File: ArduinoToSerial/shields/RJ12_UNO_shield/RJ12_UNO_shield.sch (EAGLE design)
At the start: 15 parts, among them CON1 RJ12, CON2 RJ12, CON3 RJ12, CON4 RJ12

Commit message: increased isolate space from GND plate. Fixed RX-TX connection
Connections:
- net N$15: now also U$5.TX; no longer U$5.RX
- net N$16: now also U$5.RX; no longer U$5.TX
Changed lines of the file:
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@@
 <segment>
 <pinref part="D0-D7" gate="G$1" pin="D0(RX)"/>
-<pinref part="U$5" gate="G$1" pin="RX"/>
-<wire x1="58.42" y1="0" x2="106.68" y2="0" width="0.1524" layer="91"/>
 <pinref part="D0-D1" gate="G$1" pin="D0(RX)"/>
 <wire x1="106.68" y1="0" x2="124.46" y2="0" width="0.1524" layer="91"/>
-<junction x="106.68" y="0"/>
+<pinref part="U$5" gate="G$1" pin="TX"/>
+<wire x1="58.42" y1="5.08" x2="76.2" y2="5.08" width="0.1524" layer="91"/>
+<wire x1="76.2" y1="5.08" x2="81.28" y2="0" width="0.1524" layer="91"/>
+<wire x1="81.28" y1="0" x2="106.68" y2="0" width="0.1524" layer="91"/>
 </segment>
 </net>
@@
 <segment>
 <pinref part="D0-D7" gate="G$1" pin="D1(TX)"/>
-<pinref part="U$5" gate="G$1" pin="TX"/>
-<wire x1="58.42" y1="5.08" x2="106.68" y2="5.08" width="0.1524" layer="91"/>
 <pinref part="D0-D1" gate="G$1" pin="D1(TX)"/>
 <wire x1="106.68" y1="5.08" x2="124.46" y2="5.08" width="0.1524" layer="91"/>
-<junction x="106.68" y="5.08"/>
+<wire x1="106.68" y1="5.08" x2="81.28" y2="5.08" width="0.1524" layer="91"/>
+<wire x1="81.28" y1="5.08" x2="76.2" y2="0" width="0.1524" layer="91"/>
+<pinref part="U$5" gate="G$1" pin="RX"/>
+<wire x1="76.2" y1="0" x2="58.42" y2="0" width="0.1524" layer="91"/>
 </segment>
 </net>

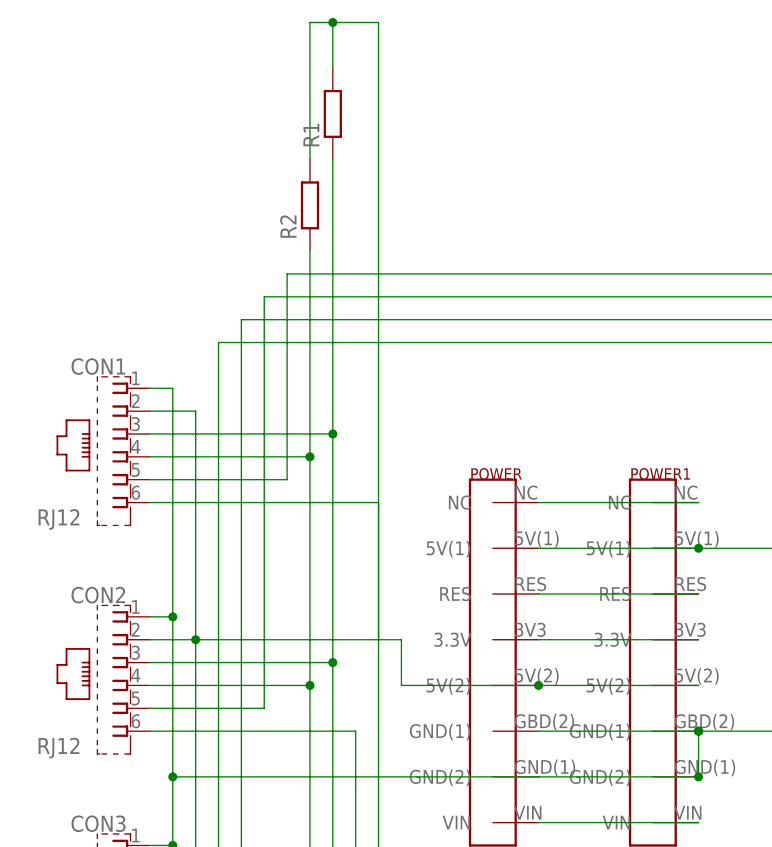
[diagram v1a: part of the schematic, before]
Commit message: added a THT resistor version
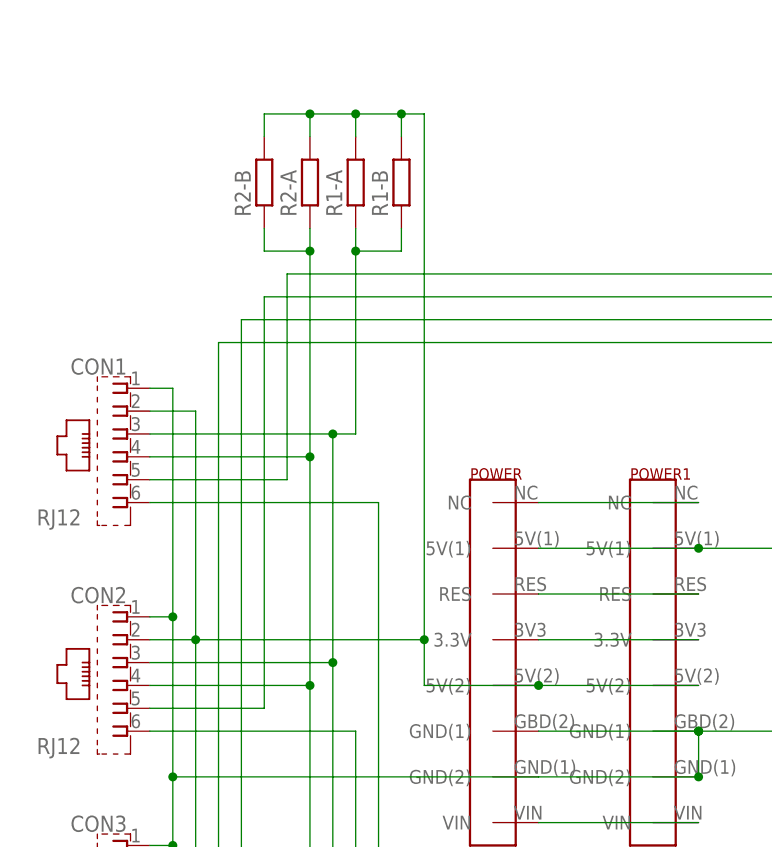
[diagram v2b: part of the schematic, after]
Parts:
- removed R1, R2: (no value), resistor:R-EU_R0805
- added R1-A, R2-A: (no value), resistor:R-EU_0207/10
- added R1-B, R2-B: (no value), resistor:R-EU_R0805W
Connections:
- net N$1: now also R1-A.1, R1-B.1; no longer R1.1
- net N$2: now also R2-A.1, R2-B.1; no longer R2.1
- net N$31: now also R1-A.2, R1-B.2, R2-A.2, R2-B.2; no longer R1.2, R2.2
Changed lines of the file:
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@@
 <part name="POWER1" library="AtoG" deviceset="POWER" device=""/>
 <part name="ANALOG1" library="AtoG" deviceset="ANALOG" device=""/>
-<part name="R1" library="resistor" deviceset="R-EU_" device="R0805"/>
-<part name="R2" library="resistor" deviceset="R-EU_" device="R0805"/>
+<part name="R1-A" library="resistor" deviceset="R-EU_" device="0207/10"/>
+<part name="R2-A" library="resistor" deviceset="R-EU_" device="0207/10"/>
+<part name="R2-B" library="resistor" deviceset="R-EU_" device="R0805W"/>
+<part name="R1-B" library="resistor" deviceset="R-EU_" device="R0805W"/>
 </parts>
 <sheets>
@@
 <instance part="POWER1" gate="G$1" x="33.02" y="50.8"/>
 <instance part="ANALOG1" gate="G$1" x="33.02" y="12.7"/>
-<instance part="R1" gate="G$1" x="-2.54" y="111.76" rot="R90"/>
-<instance part="R2" gate="G$1" x="-5.08" y="101.6" rot="R90"/>
+<instance part="R1-A" gate="G$1" x="0" y="104.14" rot="R90"/>
+<instance part="R2-A" gate="G$1" x="-5.08" y="104.14" rot="R90"/>
+<instance part="R2-B" gate="G$1" x="-10.16" y="104.14" rot="R90"/>
+<instance part="R1-B" gate="G$1" x="5.08" y="104.14" rot="R90"/>
 </instances>
 <busses>
@@
 <pinref part="CON1" gate="G$1" pin="3"/>
 <wire x1="-22.86" y1="76.2" x2="-2.54" y2="76.2" width="0.1524" layer="91"/>
-<pinref part="R1" gate="G$1" pin="1"/>
-<wire x1="-2.54" y1="106.68" x2="-2.54" y2="76.2" width="0.1524" layer="91"/>
+<pinref part="R1-A" gate="G$1" pin="1"/>
+<wire x1="0" y1="99.06" x2="0" y2="96.52" width="0.1524" layer="91"/>
 <junction x="-2.54" y="76.2"/>
+<wire x1="0" y1="96.52" x2="0" y2="76.2" width="0.1524" layer="91"/>
+<wire x1="0" y1="76.2" x2="-2.54" y2="76.2" width="0.1524" layer="91"/>
+<pinref part="R1-B" gate="G$1" pin="1"/>
+<wire x1="5.08" y1="99.06" x2="5.08" y2="96.52" width="0.1524" layer="91"/>
+<wire x1="5.08" y1="96.52" x2="0" y2="96.52" width="0.1524" layer="91"/>
+<junction x="0" y="96.52"/>
 </segment>
 </net>
@@
 <junction x="-5.08" y="22.86"/>
 <junction x="-5.08" y="48.26"/>
-<pinref part="R2" gate="G$1" pin="1"/>
+<pinref part="R2-A" gate="G$1" pin="1"/>
 <wire x1="-5.08" y1="73.66" x2="-5.08" y2="96.52" width="0.1524" layer="91"/>
 <junction x="-5.08" y="73.66"/>
+<pinref part="R2-B" gate="G$1" pin="1"/>
+<wire x1="-5.08" y1="96.52" x2="-5.08" y2="99.06" width="0.1524" layer="91"/>
+<wire x1="-5.08" y1="96.52" x2="-10.16" y2="96.52" width="0.1524" layer="91"/>
+<wire x1="-10.16" y1="96.52" x2="-10.16" y2="99.06" width="0.1524" layer="91"/>
+<junction x="-5.08" y="96.52"/>
 </segment>
 </net>
@@
 <pinref part="POWER" gate="G$1" pin="5V(2)"/>
 <wire x1="20.32" y1="48.26" x2="38.1" y2="48.26" width="0.1524" layer="91"/>
-<wire x1="20.32" y1="48.26" x2="5.08" y2="48.26" width="0.1524" layer="91"/>
-<wire x1="5.08" y1="48.26" x2="5.08" y2="53.34" width="0.1524" layer="91"/>
+<wire x1="20.32" y1="48.26" x2="7.62" y2="48.26" width="0.1524" layer="91"/>
+<wire x1="7.62" y1="48.26" x2="7.62" y2="53.34" width="0.1524" layer="91"/>
 <pinref part="CON1" gate="G$1" pin="2"/>
 <wire x1="-22.86" y1="78.74" x2="-17.78" y2="78.74" width="0.1524" layer="91"/>
@@
 <pinref part="CON3" gate="G$1" pin="2"/>
 <wire x1="-22.86" y1="27.94" x2="-17.78" y2="27.94" width="0.1524" layer="91"/>
-<wire x1="2.54" y1="53.34" x2="-17.78" y2="53.34" width="0.1524" layer="91"/>
 <junction x="-17.78" y="53.34"/>
 <junction x="-17.78" y="27.94"/>
 <junction x="20.32" y="48.26"/>
-<wire x1="5.08" y1="53.34" x2="2.54" y2="53.34" width="0.1524" layer="91"/>
-<wire x1="2.54" y1="53.34" x2="2.54" y2="121.92" width="0.1524" layer="91"/>
-<pinref part="R2" gate="G$1" pin="2"/>
-<wire x1="-5.08" y1="106.68" x2="-5.08" y2="121.92" width="0.1524" layer="91"/>
-<pinref part="R1" gate="G$1" pin="2"/>
-<wire x1="-5.08" y1="121.92" x2="-2.54" y2="121.92" width="0.1524" layer="91"/>
-<wire x1="-2.54" y1="121.92" x2="-2.54" y2="116.84" width="0.1524" layer="91"/>
-<wire x1="2.54" y1="121.92" x2="-2.54" y2="121.92" width="0.1524" layer="91"/>
-<junction x="-2.54" y="121.92"/>
-</segment>
-</net>
+<wire x1="7.62" y1="53.34" x2="-17.78" y2="53.34" width="0.1524" layer="91"/>
+<wire x1="7.62" y1="53.34" x2="7.62" y2="111.76" width="0.1524" layer="91"/>
+<pinref part="R2-A" gate="G$1" pin="2"/>
+<wire x1="-5.08" y1="109.22" x2="-5.08" y2="111.76" width="0.1524" layer="91"/>
+<pinref part="R1-A" gate="G$1" pin="2"/>
+<wire x1="-5.08" y1="111.76" x2="0" y2="111.76" width="0.1524" layer="91"/>
+<wire x1="0" y1="111.76" x2="0" y2="109.22" width="0.1524" layer="91"/>
+<wire x1="7.62" y1="111.76" x2="5.08" y2="111.76" width="0.1524" layer="91"/>
+<junction x="0" y="111.76"/>
+<junction x="7.62" y="53.34"/>
+<pinref part="R1-B" gate="G$1" pin="2"/>
+<wire x1="5.08" y1="111.76" x2="0" y2="111.76" width="0.1524" layer="91"/>
+<wire x1="5.08" y1="109.22" x2="5.08" y2="111.76" width="0.1524" layer="91"/>
+<pinref part="R2-B" gate="G$1" pin="2"/>
+<wire x1="-5.08" y1="111.76" x2="-10.16" y2="111.76" width="0.1524" layer="91"/>
+<wire x1="-10.16" y1="111.76" x2="-10.16" y2="109.22" width="0.1524" layer="91"/>
+<junction x="5.08" y="111.76"/>
+<junction x="-5.08" y="111.76"/>
+</segment>
+</net>
